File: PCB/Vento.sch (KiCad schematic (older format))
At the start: 0 parts

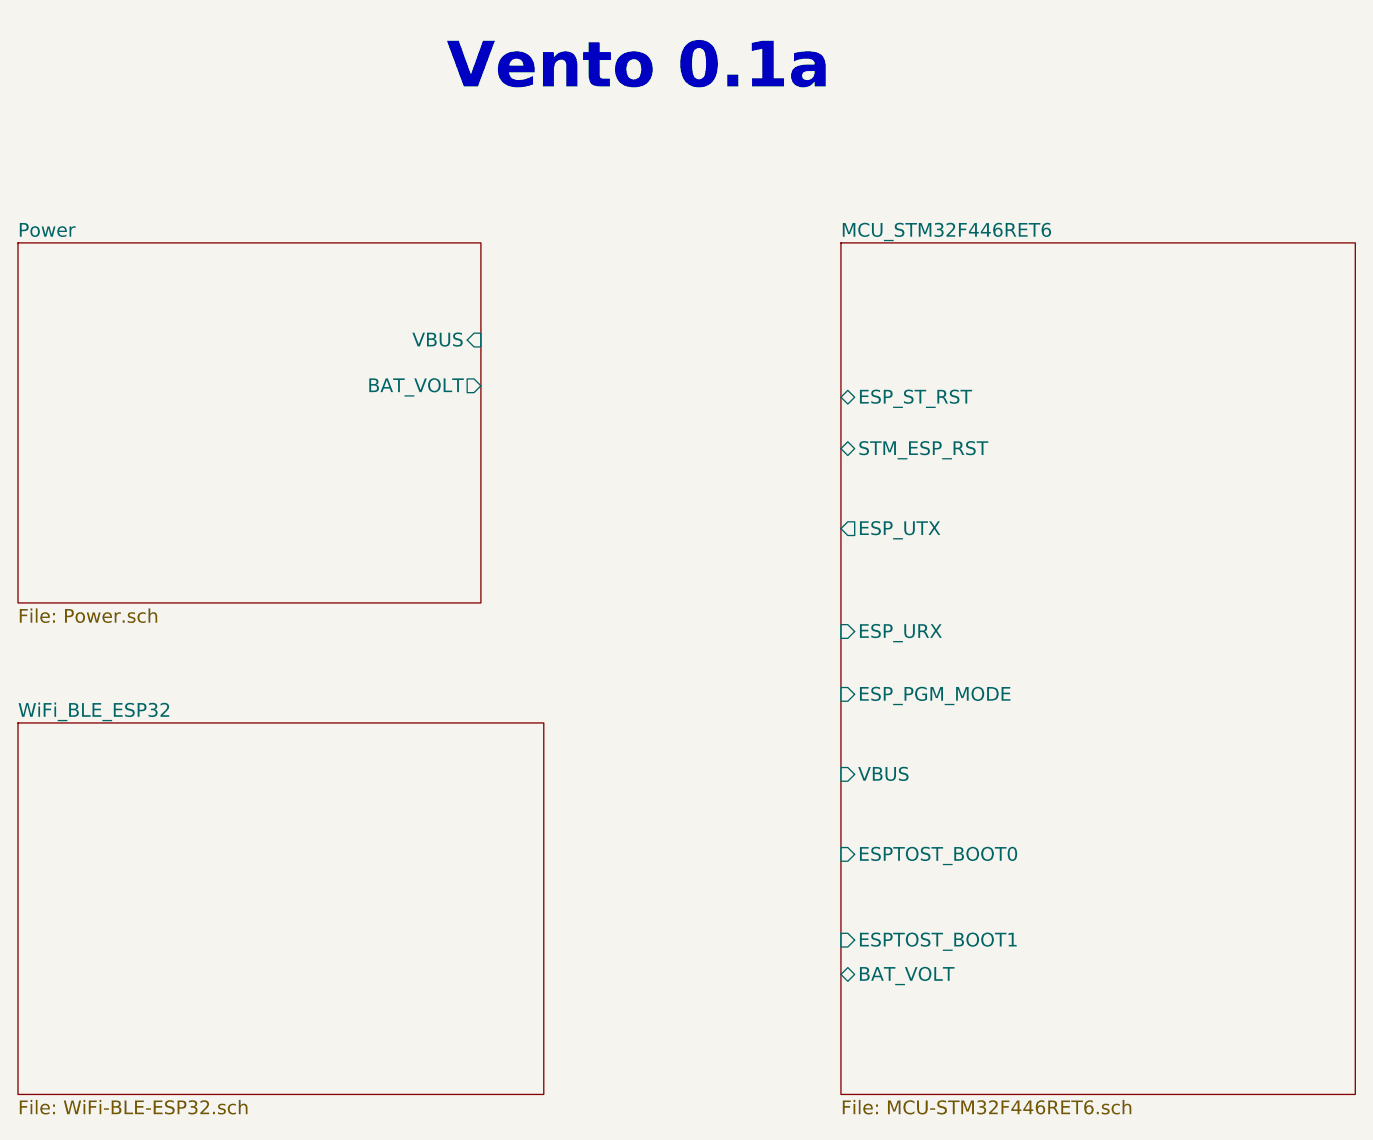
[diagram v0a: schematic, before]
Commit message: Schematic Done, Board Underway
Schematic completed. STM32 section upated from Aria project schematic,
ESP32 schematic completed with the help of reference schematic.
Datasheets for componens used also added. The PCB is near complete, Aria
was improted and modifed to speed up the process. More to come!
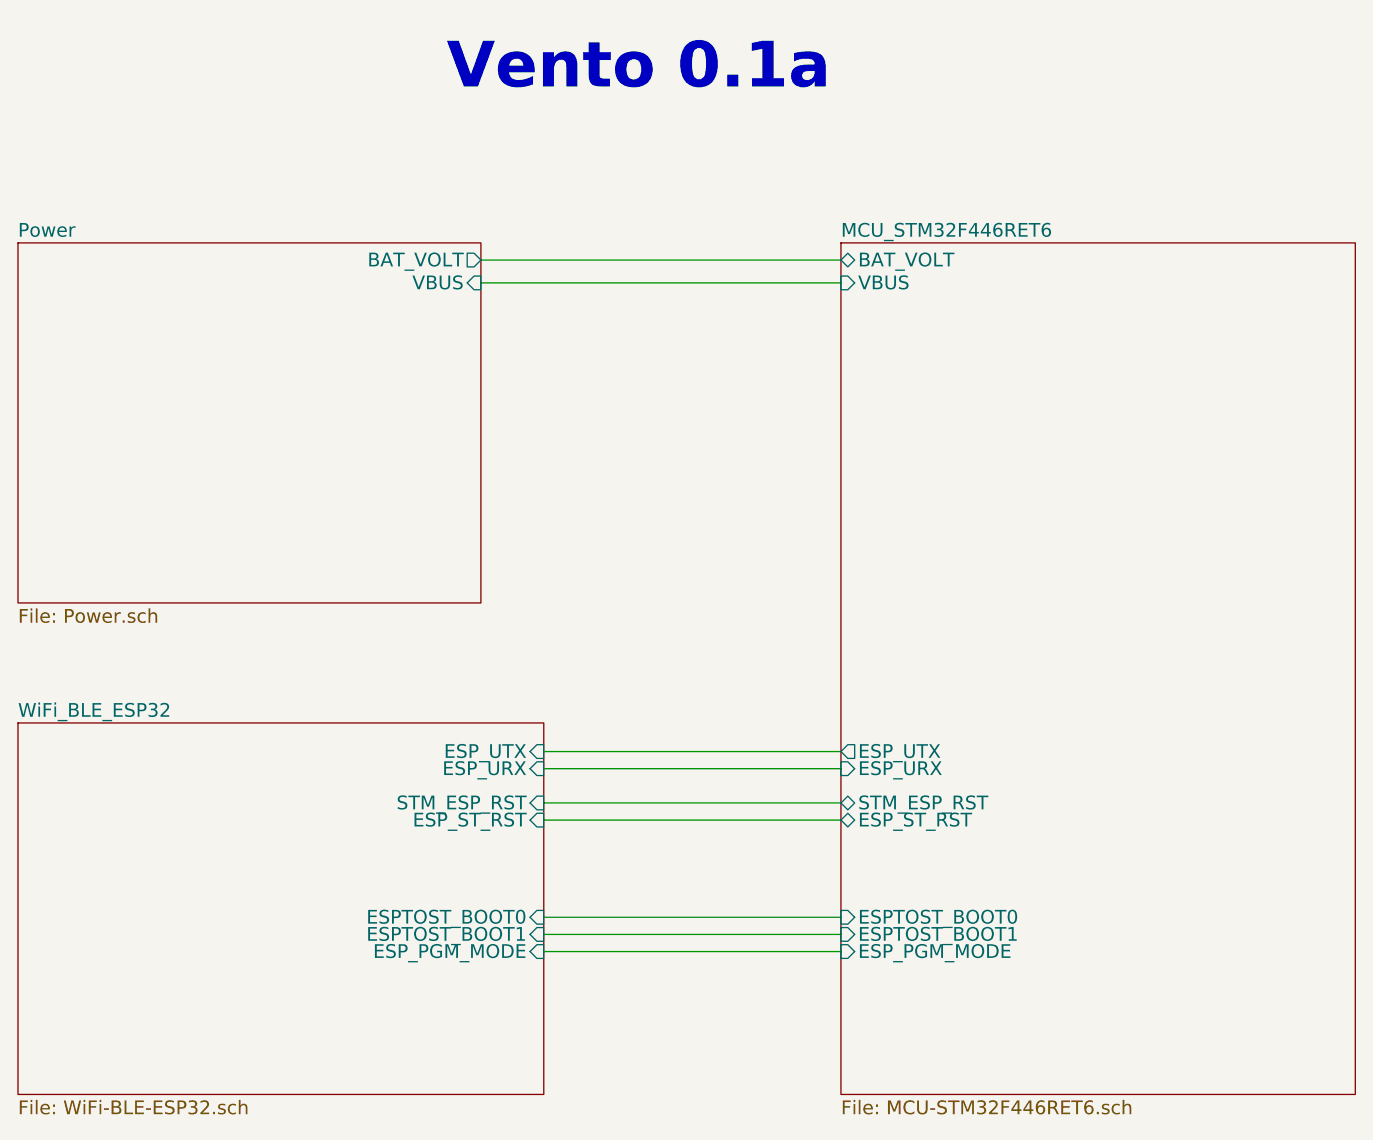
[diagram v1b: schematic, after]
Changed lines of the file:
@@
 F0 "MCU_STM32F446RET6" 60
 F1 "MCU-STM32F446RET6.sch" 60
-F2 "ESP_ST_RST" B L 7000 2575 60
-F3 "STM_ESP_RST" B L 7000 2800 60
-F4 "ESP_UTX" O L 7000 3150 60
-F5 "ESP_URX" I L 7000 3600 60
-F6 "ESP_PGM_MODE" I L 7000 3875 60
-F7 "VBUS" I L 7000 4225 60
-F8 "ESPTOST_BOOT0" I L 7000 4575 60
-F9 "ESPTOST_BOOT1" I L 7000 4950 60
-F10 "BAT_VOLT" B L 7000 5100 60
+F2 "ESP_ST_RST" B L 7000 4425 60
+F3 "STM_ESP_RST" B L 7000 4350 60
+F4 "ESP_UTX" O L 7000 4125 60
+F5 "ESP_URX" I L 7000 4200 60
+F6 "ESP_PGM_MODE" I L 7000 5000 60
+F7 "VBUS" I L 7000 2075 60
+F8 "ESPTOST_BOOT0" I L 7000 4850 60
+F9 "ESPTOST_BOOT1" I L 7000 4925 60
+F10 "BAT_VOLT" B L 7000 1975 60
 $EndSheet
 $Sheet
@@
 F0 "Power" 60
 F1 "Power.sch" 60
-F2 "VBUS" I R 5425 2325 60
-F3 "BAT_VOLT" O R 5425 2525 60
+F2 "VBUS" I R 5425 2075 60
+F3 "BAT_VOLT" O R 5425 1975 60
 $EndSheet
 $Sheet
@@
 F0 "WiFi_BLE_ESP32" 60
 F1 "WiFi-BLE-ESP32.sch" 60
+F2 "ESP_UTX" I R 5700 4125 60
+F3 "ESP_URX" I R 5700 4200 60
+F4 "STM_ESP_RST" I R 5700 4350 60
+F5 "ESP_PGM_MODE" I R 5700 5000 60
+F6 "ESPTOST_BOOT0" I R 5700 4850 60
+F7 "ESPTOST_BOOT1" I R 5700 4925 60
+F8 "ESP_ST_RST" I R 5700 4425 60
 $EndSheet
 Text Notes 5275 1250 0    200  ~ 40
 Vento 0.1a
+Wire Wire Line
+	5425 1975 7000 1975
+Wire Wire Line
+	5425 2075 7000 2075
+Wire Wire Line
+	7000 4425 5700 4425
+Wire Wire Line
+	5700 4350 7000 4350
+Wire Wire Line
+	7000 4200 5700 4200
+Wire Wire Line
+	5700 4125 7000 4125
+Wire Wire Line
+	7000 4850 5700 4850
+Wire Wire Line
+	5700 4925 7000 4925
+Wire Wire Line
+	7000 5000 5700 5000
 $EndSCHEMATC
